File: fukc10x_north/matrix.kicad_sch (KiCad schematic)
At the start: 237 parts

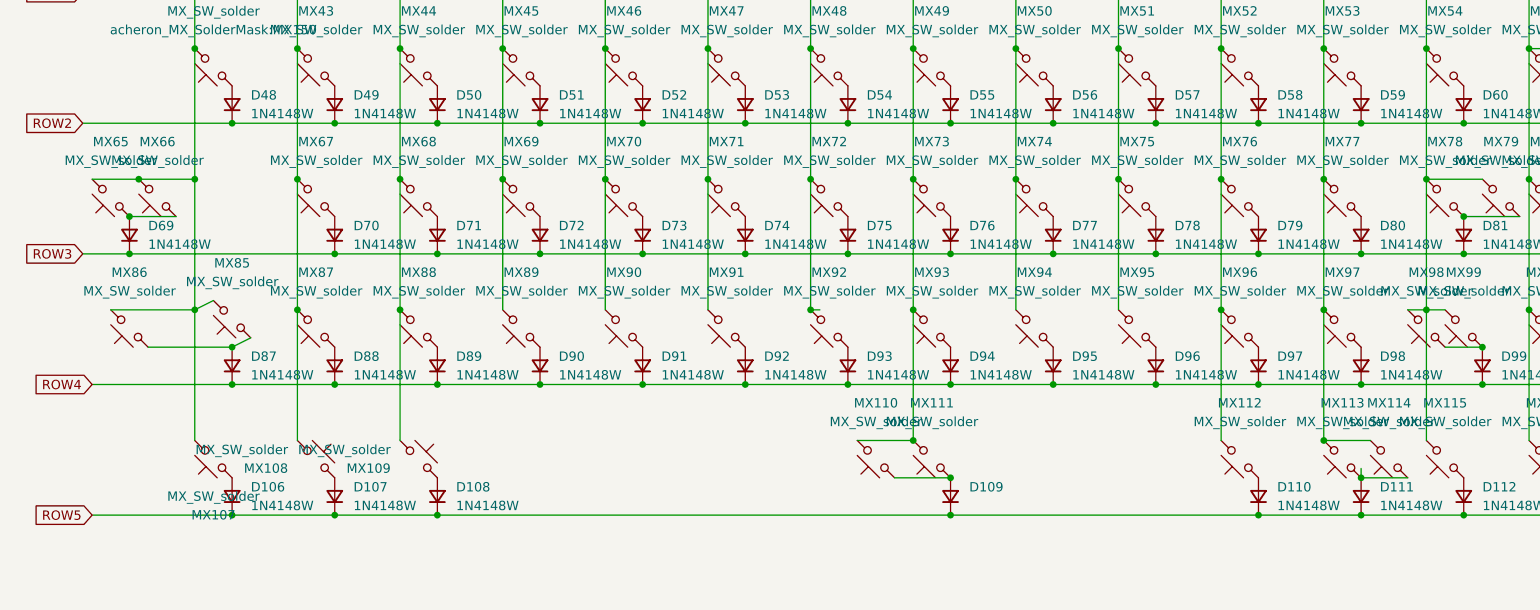
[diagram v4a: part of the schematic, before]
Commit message: adjusted some traces, flipped some switches, went through drc again
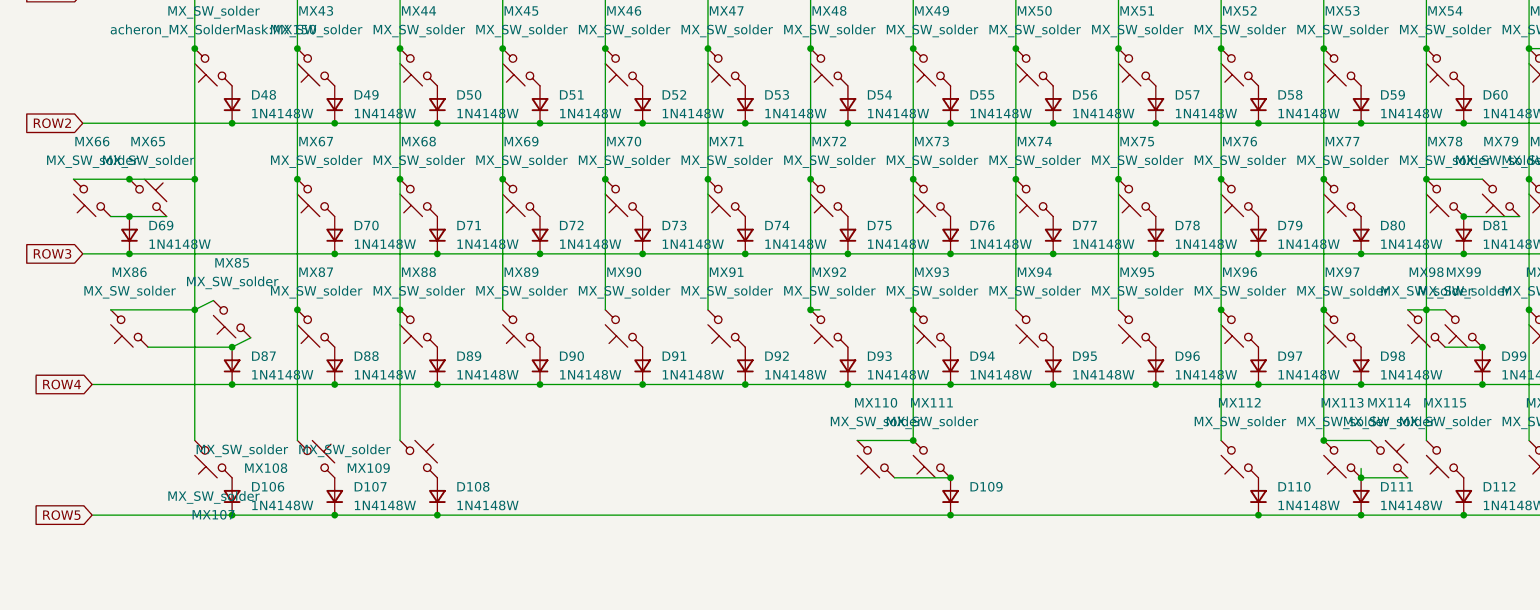
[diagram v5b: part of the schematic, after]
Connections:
- net COL0: now also MX65.1; no longer MX65.2
- net COL11: now also MX114.1; no longer MX114.2
- net at D69.2 (A), MX66.1: now also MX65.2; no longer MX65.1
- net at D111.2 (A), MX113.1: now also MX114.2; no longer MX114.1
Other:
- moved on the sheet: MX114, MX65, MX66
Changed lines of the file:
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@@
 	)
 	(junction
-		(at 29.21 90.17)
-		(diameter 0)
-		(color 0 0 0 0)
-	)
-	(junction
 		(at 78.74 90.17)
 		(diameter 0)
@@
 	)
 	(junction
-		(at 27.94 95.25)
-		(diameter 0)
-		(color 0 0 0 0)
-	)
-	(junction
 		(at 97.79 64.77)
 		(diameter 0)
@@
 	)
 	(junction
+		(at 27.94 90.17)
+		(diameter 0)
+		(color 0 0 0 0)
+	)
+	(junction
 		(at 247.65 135.89)
 		(diameter 0)
@@
 	)
 	(junction
+		(at 27.94 95.25)
+		(diameter 0)
+		(color 0 0 0 0)
+	)
+	(junction
 		(at 360.68 77.47)
 		(diameter 0)
@@
 	(wire
 		(pts
+			(xy 20.32 90.17) (xy 27.94 90.17)
+		)
+		(stroke
+			(width 0)
+			(type default)
+		)
+	)
+	(wire
+		(pts
 			(xy 195.58 135.89) (xy 209.55 135.89)
 		)
@@
 	(wire
 		(pts
-			(xy 22.86 90.17) (xy 29.21 90.17)
-		)
-		(stroke
-			(width 0)
-			(type default)
-		)
-	)
-	(wire
-		(pts
 			(xy 125.73 82.55) (xy 139.7 82.55)
 		)
@@
 	(wire
 		(pts
-			(xy 27.94 95.25) (xy 34.29 95.25)
+			(xy 27.94 95.25) (xy 25.4 95.25)
 		)
 		(stroke
@@
 	(wire
 		(pts
+			(xy 27.94 90.17) (xy 36.83 90.17)
+		)
+		(stroke
+			(width 0)
+			(type default)
+		)
+	)
+	(wire
+		(pts
 			(xy 256.54 107.95) (xy 256.54 125.73)
 		)
@@
 	(wire
 		(pts
-			(xy 29.21 90.17) (xy 36.83 90.17)
-		)
-		(stroke
-			(width 0)
-			(type default)
-		)
-	)
-	(wire
-		(pts
 			(xy 148.59 33.02) (xy 148.59 54.61)
 		)
@@
 	(wire
 		(pts
+			(xy 33.02 95.25) (xy 27.94 95.25)
+		)
+		(stroke
+			(width 0)
+			(type default)
+		)
+	)
+	(wire
+		(pts
 			(xy 275.59 64.77) (xy 299.72 64.77)
 		)
@@
 	(symbol
 		(lib_id "PCM_marbastlib-mx:MX_SW_solder")
-		(at 25.4 92.71 180)
+		(at 30.48 92.71 0)
 		(unit 1)
 		(body_style 1)
@@
 		(fields_autoplaced yes)
 		(property "Reference" "MX65"
-			(at 25.4 85.09 0)
+			(at 30.48 85.09 0)
 			(show_name no)
 			(do_not_autoplace no)
@@
 		)
 		(property "Value" "MX_SW_solder"
-			(at 25.4 87.63 0)
+			(at 30.48 87.63 0)
 			(show_name no)
 			(do_not_autoplace no)
@@
 		)
 		(property "Footprint" "acheron_MX_SolderMask:MX175"
-			(at 25.4 92.71 0)
+			(at 30.48 92.71 0)
 			(hide yes)
 			(show_name no)
@@
 		)
 		(property "Datasheet" ""
-			(at 25.4 92.71 0)
+			(at 30.48 92.71 0)
 			(hide yes)
 			(show_name no)
@@
 		)
 		(property "Description" "Push button switch, normally open, two pins, 45° tilted"
-			(at 25.4 92.71 0)
+			(at 30.48 92.71 0)
 			(hide yes)
 			(show_name no)
@@
 	(symbol
 		(lib_id "PCM_marbastlib-mx:MX_SW_solder")
-		(at 199.39 128.27 180)
+		(at 199.39 128.27 0)
 		(unit 1)
 		(body_style 1)
@@
 	(symbol
 		(lib_id "PCM_marbastlib-mx:MX_SW_solder")
-		(at 31.75 92.71 180)
+		(at 22.86 92.71 180)
 		(unit 1)
 		(body_style 1)
@@
 		(fields_autoplaced yes)
 		(property "Reference" "MX66"
-			(at 31.75 85.09 0)
+			(at 22.86 85.09 0)
 			(show_name no)
 			(do_not_autoplace no)
@@
 		)
 		(property "Value" "MX_SW_solder"
-			(at 31.75 87.63 0)
+			(at 22.86 87.63 0)
 			(show_name no)
 			(do_not_autoplace no)
@@
 		)
 		(property "Footprint" "acheron_MX_SolderMask:MX125"
-			(at 31.75 92.71 0)
+			(at 22.86 92.71 0)
 			(hide yes)
 			(show_name no)
@@
 		)
 		(property "Datasheet" ""
-			(at 31.75 92.71 0)
+			(at 22.86 92.71 0)
 			(hide yes)
 			(show_name no)
@@
 		)
 		(property "Description" "Push button switch, normally open, two pins, 45° tilted"
-			(at 31.75 92.71 0)
+			(at 22.86 92.71 0)
 			(hide yes)
 			(show_name no)

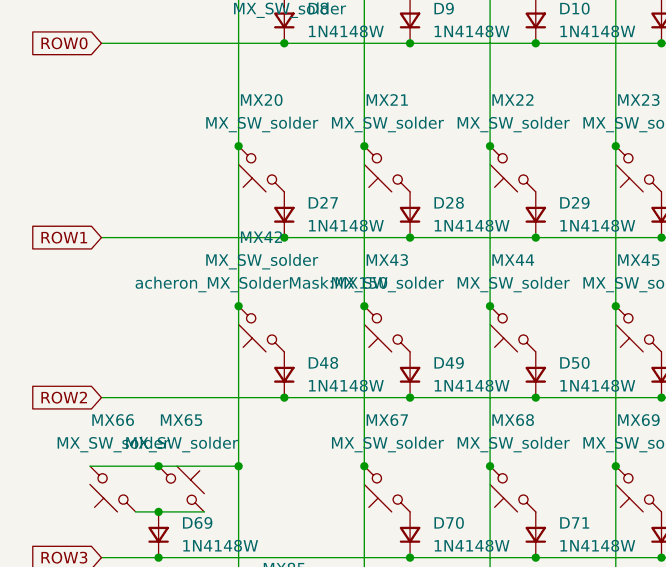
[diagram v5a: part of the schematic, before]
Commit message: changed to mx alps footprints. Alexandria footrpints were edited for this putpose. Added those footprint to the library folder
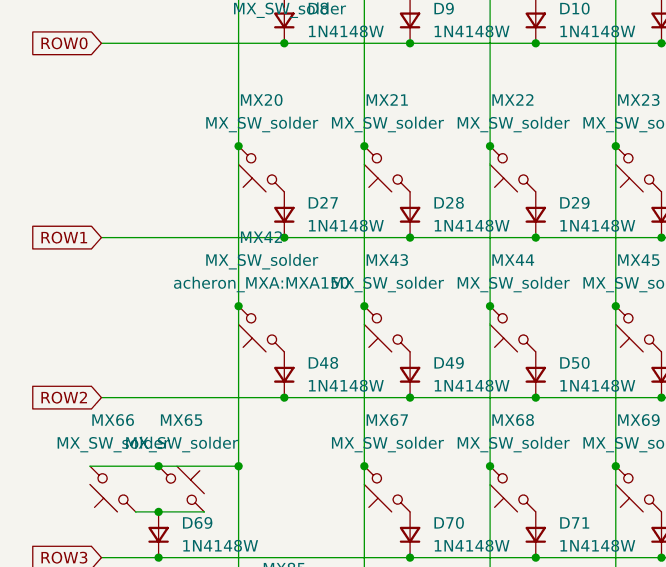
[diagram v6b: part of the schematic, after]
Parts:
- MX1, MX10, MX100, MX101, MX102, MX103, MX104, MX106, MX108, MX11, MX114, MX115, MX117, MX118, MX119, MX12, MX121, MX122, MX123, MX124, MX13, MX14, MX15, MX16, MX17, MX18, MX19, MX2, MX20, MX21, MX22, MX23, MX24, MX25, MX26, MX27, MX28, MX29, MX3, MX30, MX31, MX32, MX33, MX35, MX36, MX37, MX38, MX39, MX4, MX40, MX41, MX43, MX44, MX45, MX46, MX47, MX48, MX49, MX5, MX50, MX51, MX52, MX53, MX54, MX57, MX58, MX59, MX6, MX60, MX61, MX62, MX64, MX67, MX68, MX69, MX7, MX70, MX71, MX72, MX73, MX74, MX75, MX76, MX77, MX78, MX8, MX80, MX81, MX82, MX83, MX84, MX87, MX88, MX89, MX9, MX90, MX91, MX92, MX93, MX94, MX95, MX96, MX97: footprint acheron_MX_SolderMask:MX100 -> acheron_MXA:MXA100
- MX105, MX63: footprint acheron_MX_SolderMask:MX200V -> acheron_MXA:MXA200V
- MX107, MX109, MX112, MX113, MX116, MX42, MX55: footprint acheron_MX_SolderMask:MX150 -> acheron_MXA:MXA150
- MX110: footprint acheron_MX_SolderMask:MX600CR -> acheron_MXA:MXA600R
- MX111: footprint acheron_MX_SolderMask:MX700R -> acheron_MXA:MXA700R
- MX120: footprint acheron_MX_SolderMask:MX200R -> acheron_MXA:MXA200R
- MX34: footprint acheron_MX_SolderMask:MX250 -> acheron_MXA:MXA250
- MX56: footprint acheron_MX_SolderMask:MX_ISOEnter -> acheron_MXA:MXA_ISO_Enter
- MX65, MX98: footprint acheron_MX_SolderMask:MX175 -> acheron_MXA:MXA175
- MX66, MX86: footprint acheron_MX_SolderMask:MX125 -> acheron_MXA:MXA125
- MX79: footprint acheron_MX_SolderMask:MX225R -> acheron_MXA:MXA225R
- MX85: footprint acheron_MX_SolderMask:MX225 -> acheron_MXA:MXA225
- MX99: footprint acheron_MX_SolderMask:MX275 -> acheron_MXA:MXA275

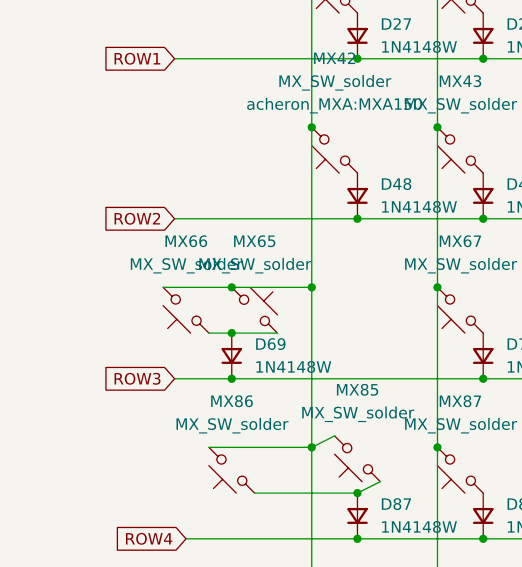
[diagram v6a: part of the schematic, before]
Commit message: cursed alps capslock added (1.5u w step) added outline dxf
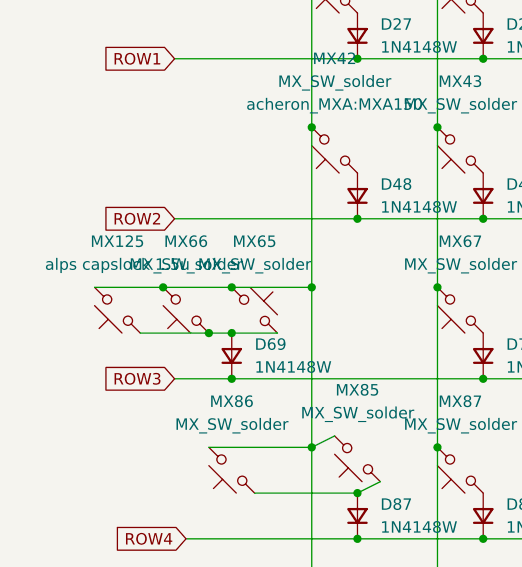
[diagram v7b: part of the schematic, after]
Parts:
- added MX125: alps capslock 1.5u, PCM_marbastlib-xp-alps:SW_Alps_1.75u_STP_1.5, symbol PCM_marbastlib-mx:MX_SW_solder
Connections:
- net COL0: now also MX125.2
- net at D69.2 (A), MX65.2, MX66.1: now also MX125.1
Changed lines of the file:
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@@
 	)
 	(junction
+		(at 25.4 95.25)
+		(diameter 0)
+		(color 0 0 0 0)
+	)
+	(junction
 		(at 223.52 82.55)
 		(diameter 0)
@@
 	)
 	(junction
+		(at 20.32 90.17)
+		(diameter 0)
+		(color 0 0 0 0)
+	)
+	(junction
 		(at 204.47 54.61)
 		(diameter 0)
@@
 	(wire
 		(pts
+			(xy 12.7 90.17) (xy 20.32 90.17)
+		)
+		(stroke
+			(width 0)
+			(type default)
+		)
+	)
+	(wire
+		(pts
 			(xy 204.47 90.17) (xy 204.47 107.95)
 		)
@@
 	(wire
 		(pts
+			(xy 17.78 95.25) (xy 25.4 95.25)
+		)
+		(stroke
+			(width 0)
+			(type default)
+		)
+	)
+	(wire
+		(pts
 			(xy 27.94 90.17) (xy 36.83 90.17)
 		)
@@
 					(unit 1)
 				)
+			)
+		)
+	)
+	(symbol
+		(lib_id "PCM_marbastlib-mx:MX_SW_solder")
+		(at 15.24 92.71 180)
+		(unit 1)
+		(body_style 1)
+		(exclude_from_sim no)
+		(in_bom no)
+		(on_board yes)
+		(in_pos_files yes)
+		(dnp no)
+		(fields_autoplaced yes)
+		(property "Reference" "MX125"
+			(at 15.24 85.09 0)
+			(show_name no)
+			(do_not_autoplace no)
+			(effects
+				(font
+					(size 1.27 1.27)
+				)
+			)
+		)
+		(property "Value" "alps capslock 1.5u"
+			(at 15.24 87.63 0)
+			(show_name no)
+			(do_not_autoplace no)
+			(effects
+				(font
+					(size 1.27 1.27)
+				)
+			)
+		)
+		(property "Footprint" "PCM_marbastlib-xp-alps:SW_Alps_1.75u_STP_1.5"
+			(at 15.24 92.71 0)
+			(hide yes)
+			(show_name no)
+			(do_not_autoplace no)
+			(effects
+				(font
+					(size 1.27 1.27)
+				)
+			)
+		)
+		(property "Datasheet" ""
+			(at 15.24 92.71 0)
+			(hide yes)
+			(show_name no)
+			(do_not_autoplace no)
+			(effects
+				(font
+					(size 1.27 1.27)
+				)
+			)
+		)
+		(property "Description" "Push button switch, normally open, two pins, 45° tilted"
+			(at 15.24 92.71 0)
+			(hide yes)
+			(show_name no)
+			(do_not_autoplace no)
+			(effects
+				(font
+					(size 1.27 1.27)
+				)
+			)
+		)
+		(pin "1"
+		)
+		(pin "2"
+		)
+		(instances
+			(project "fukc10x_north"
+				(path "/e8620368-78e2-44a1-a371-0f1795fb4009/465de3a7-4d93-4533-8b78-49078295a82f"
+					(reference "MX125")
+					(unit 1)
+				)

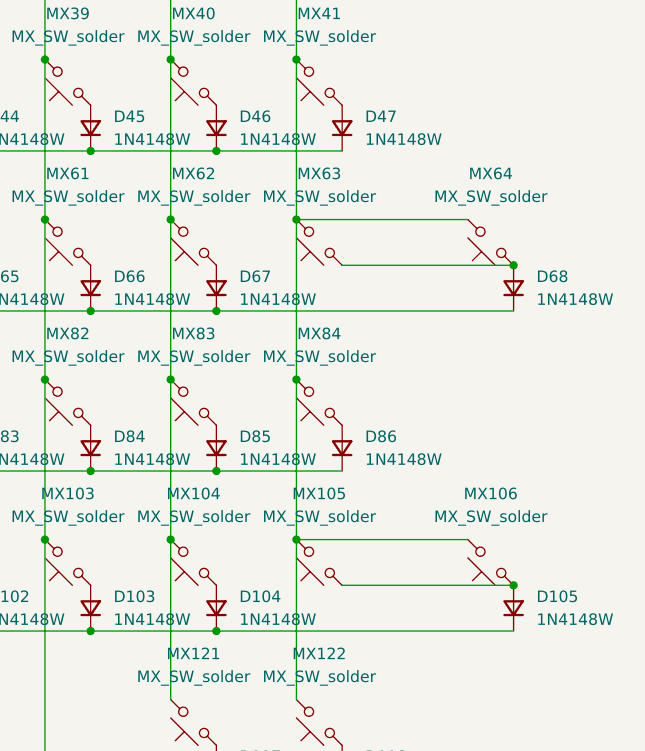
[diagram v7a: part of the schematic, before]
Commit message: changed vertical 2us on numpad. MX and alps switches for those are now separat footprints to make routing easier and not have cursed vertical mx switches. Adjustes some traces and so on. alps footprints are from the marbastler lib
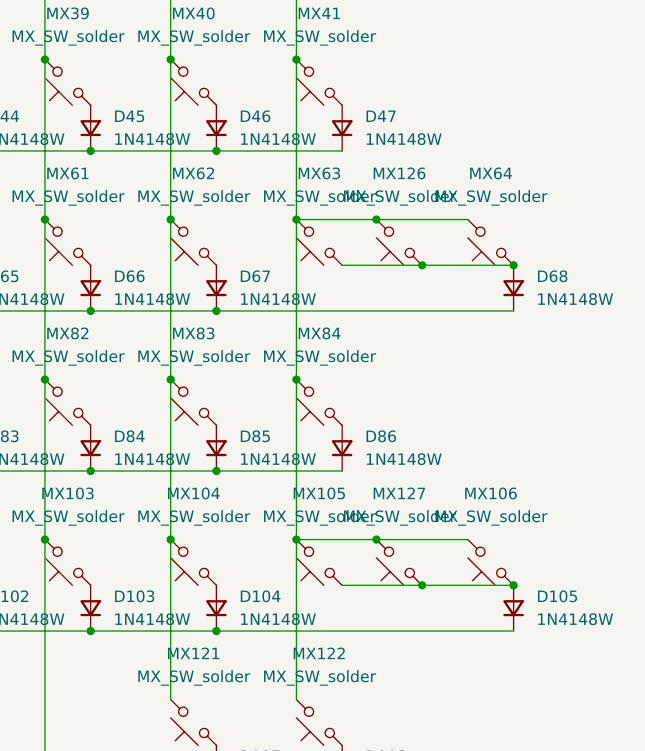
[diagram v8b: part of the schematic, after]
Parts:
- added MX126, MX127: MX_SW_solder, PCM_marbastlib-xp-alps:SW_Alps_1u, symbol PCM_marbastlib-mx:MX_SW_solder
- MX105, MX63: footprint acheron_MXA:MXA200V -> acheron_MX:MX200V
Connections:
- net COL20: now also MX126.2, MX127.2
- net at D105.2 (A), MX105.1, MX106.1: now also MX127.1
- net at D68.2 (A), MX63.1, MX64.1: now also MX126.1
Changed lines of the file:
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@@
 	)
 	(junction
+		(at 345.44 107.95)
+		(diameter 0)
+		(color 0 0 0 0)
+	)
+	(junction
 		(at 162.56 54.61)
 		(diameter 0)
@@
 	)
 	(junction
+		(at 350.52 113.03)
+		(diameter 0)
+		(color 0 0 0 0)
+	)
+	(junction
 		(at 308.61 54.61)
 		(diameter 0)
@@
 	)
 	(junction
+		(at 345.44 72.39)
+		(diameter 0)
+		(color 0 0 0 0)
+	)
+	(junction
 		(at 195.58 118.11)
 		(diameter 0)
@@
 	)
 	(junction
+		(at 350.52 77.47)
+		(diameter 0)
+		(color 0 0 0 0)
+	)
+	(junction
 		(at 181.61 64.77)
 		(diameter 0)
@@
 	(wire
 		(pts
+			(xy 345.44 72.39) (xy 355.6 72.39)
+		)
+		(stroke
+			(width 0)
+			(type default)
+		)
+	)
+	(wire
+		(pts
 			(xy 209.55 135.89) (xy 223.52 135.89)
 		)
@@
 	(wire
 		(pts
-			(xy 336.55 107.95) (xy 355.6 107.95)
+			(xy 336.55 107.95) (xy 345.44 107.95)
 		)
 		(stroke
@@
 	(wire
 		(pts
-			(xy 341.63 77.47) (xy 360.68 77.47)
+			(xy 341.63 77.47) (xy 350.52 77.47)
+		)
+		(stroke
+			(width 0)
+			(type default)
+		)
+	)
+	(wire
+		(pts
+			(xy 345.44 107.95) (xy 355.6 107.95)
 		)
 		(stroke
@@
 	(wire
 		(pts
-			(xy 336.55 72.39) (xy 355.6 72.39)
+			(xy 336.55 72.39) (xy 345.44 72.39)
 		)
 		(stroke
@@
 	(wire
 		(pts
-			(xy 341.63 113.03) (xy 360.68 113.03)
+			(xy 341.63 113.03) (xy 350.52 113.03)
 		)
 		(stroke
@@
 	(wire
 		(pts
+			(xy 350.52 113.03) (xy 360.68 113.03)
+		)
+		(stroke
+			(width 0)
+			(type default)
+		)
+	)
+	(wire
+		(pts
 			(xy 167.64 82.55) (xy 181.61 82.55)
 		)
@@
 	(wire
 		(pts
+			(xy 350.52 77.47) (xy 360.68 77.47)
+		)
+		(stroke
+			(width 0)
+			(type default)
+		)
+	)
+	(wire
+		(pts
 			(xy 41.91 82.55) (xy 55.88 82.55)
 		)
@@
 	(symbol
 		(lib_id "PCM_marbastlib-mx:MX_SW_solder")
+		(at 347.98 110.49 180)
+		(unit 1)
+		(body_style 1)
+		(exclude_from_sim no)
+		(in_bom no)
+		(on_board yes)
+		(in_pos_files yes)
+		(dnp no)
+		(fields_autoplaced yes)
+		(property "Reference" "MX127"
+			(at 347.98 102.87 0)
+			(show_name no)
+			(do_not_autoplace no)
+			(effects
+				(font
+					(size 1.27 1.27)
+				)
+			)
+		)
+		(property "Value" "MX_SW_solder"
+			(at 347.98 105.41 0)
+			(show_name no)
+			(do_not_autoplace no)
+			(effects
+				(font
+					(size 1.27 1.27)
+				)
+			)
+		)
+		(property "Footprint" "PCM_marbastlib-xp-alps:SW_Alps_1u"
+			(at 347.98 110.49 0)
+			(hide yes)
+			(show_name no)
+			(do_not_autoplace no)
+			(effects
+				(font
+					(size 1.27 1.27)
+				)
+			)
+		)
+		(property "Datasheet" ""
+			(at 347.98 110.49 0)
+			(hide yes)
+			(show_name no)
+			(do_not_autoplace no)
+			(effects
+				(font
+					(size 1.27 1.27)
+				)
+			)
+		)
+		(property "Description" "Push button switch, normally open, two pins, 45° tilted"
+			(at 347.98 110.49 0)
+			(hide yes)
+			(show_name no)
+			(do_not_autoplace no)
+			(effects
+				(font
+					(size 1.27 1.27)
+				)
+			)
+		)
+		(pin "1"
+		)
+		(pin "2"
+		)
+		(instances
+			(project "fukc10x_north"
+				(path "/e8620368-78e2-44a1-a371-0f1795fb4009/465de3a7-4d93-4533-8b78-49078295a82f"
+					(reference "MX127")
+					(unit 1)
+				)
+			)
+		)
+	)
+	(symbol
+		(lib_id "PCM_marbastlib-mx:MX_SW_solder")
 		(at 339.09 35.56 180)
 		(unit 1)
@@
 			)
 		)
-		(property "Footprint" "acheron_MXA:MXA200V"
+		(property "Footprint" "acheron_MX:MX200V"
 			(at 339.09 110.49 0)
 			(hide yes)
@@
 	(symbol
 		(lib_id "PCM_marbastlib-mx:MX_SW_solder")
+		(at 347.98 74.93 180)
+		(unit 1)
+		(body_style 1)
+		(exclude_from_sim no)
+		(in_bom no)
+		(on_board yes)
+		(in_pos_files yes)
+		(dnp no)
+		(fields_autoplaced yes)
+		(property "Reference" "MX126"
+			(at 347.98 67.31 0)
+			(show_name no)
+			(do_not_autoplace no)
+			(effects
+				(font
+					(size 1.27 1.27)
+				)
+			)
+		)
+		(property "Value" "MX_SW_solder"
+			(at 347.98 69.85 0)
+			(show_name no)
+			(do_not_autoplace no)
+			(effects
+				(font
+					(size 1.27 1.27)
+				)
+			)
+		)
+		(property "Footprint" "PCM_marbastlib-xp-alps:SW_Alps_1u"
+			(at 347.98 74.93 0)
+			(hide yes)
+			(show_name no)
+			(do_not_autoplace no)
+			(effects
+				(font
+					(size 1.27 1.27)
+				)
+			)
+		)
+		(property "Datasheet" ""
+			(at 347.98 74.93 0)
+			(hide yes)
+			(show_name no)
+			(do_not_autoplace no)
+			(effects
+				(font
+					(size 1.27 1.27)
+				)
+			)
+		)
+		(property "Description" "Push button switch, normally open, two pins, 45° tilted"
+			(at 347.98 74.93 0)
+			(hide yes)
+			(show_name no)
+			(do_not_autoplace no)
+			(effects
+				(font
+					(size 1.27 1.27)
+				)
+			)
+		)
+		(pin "1"
+		)
+		(pin "2"
+		)
+		(instances
+			(project "fukc10x_north"
+				(path "/e8620368-78e2-44a1-a371-0f1795fb4009/465de3a7-4d93-4533-8b78-49078295a82f"
+					(reference "MX126")
+					(unit 1)
+				)
+			)
+		)
+	)
+	(symbol
+		(lib_id "PCM_marbastlib-mx:MX_SW_solder")
 		(at 207.01 74.93 180)
 		(unit 1)
@@
 			)
 		)
-		(property "Footprint" "acheron_MXA:MXA200V"
+		(property "Footprint" "acheron_MX:MX200V"
 			(at 339.09 74.93 0)
 			(hide yes)
